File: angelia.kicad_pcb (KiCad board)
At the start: 2 copper layers, 160 x 120 mm, 206 parts, among them J10 Conn_Coaxial, J15 Conn_02x05_Top_Bottom, J16 Conn_02x13_Top_Bottom, J18 Conn_02x05_Top_Bottom, J25 Conn_Coaxial, J3 Conn_Coaxial, J5 Conn_Coaxial, P1 Conn_02x05_Top_Bottom, P2 Conn_02x05_Top_Bottom, U10 LTC2208xUP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

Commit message: all decoupling done
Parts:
- C104, C124, C141, C15, C189, C19, C190, C208, C230, C235, C236, C237, C238, C240, C241, C26, C53, C69, C71, C85, C86: moved to B.Cu
- moved C154 184.5 mm to (68.2, 118.4)
- moved C157 183.1 mm to (68.0, 121.4)
- moved C155 183.0 mm to (68.2, 115.6)
- moved C162 175.6 mm to (88.0, 113.6)
- moved C163 172.7 mm to (88.0, 109.0)
- moved C218 164.9 mm to (93.7, 122.2)
- moved C233 160.5 mm to (116.2, 131.2)
- moved C183 155.5 mm to (104.4, 124.8)
- moved C197 153.1 mm to (103.2, 128.8), turned to 90 degrees
- moved C193 150.9 mm to (104.4, 122.2)
- moved C95 150.4 mm to (86.2, 81.4), turned to 90 degrees
- moved C96 148.0 mm to (88.4, 81.4), turned to 90 degrees
- moved C225 141.2 mm to (159.4, 145.6)
- moved C211 126.9 mm to (158.2, 149.2), turned to 90 degrees
- moved C230 122.1 mm to (172.4, 140.6), turned to 180 degrees
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
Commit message: beginning special components
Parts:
- removed R1: R_Small, Resistor_SMD:R_0805_2012Metric
- added C103: 1n, Capacitor_SMD:C_0805_2012Metric, F.Cu at (254.3, 61.0)
- added C105: 100p, Capacitor_SMD:C_0805_2012Metric, F.Cu at (254.3, 64.0)
- added C107: 1n, Capacitor_SMD:C_0805_2012Metric, F.Cu at (258.8, 46.0)
- added C121: 10n, Capacitor_SMD:C_0402_1005Metric, B.Cu at (152.2, 66.2)
- added C130: 10n, Capacitor_SMD:C_0402_1005Metric, B.Cu at (129.0, 72.6)
- added C131: 10n, Capacitor_SMD:C_0402_1005Metric, B.Cu at (142.0, 71.7)
- added C136: 10n, Capacitor_SMD:C_0402_1005Metric, B.Cu at (153.6, 71.8)
- added C140: 10n, Capacitor_SMD:C_0402_1005Metric, B.Cu at (129.0, 71.2)
- added C165: 10u, Capacitor_SMD:C_0805_2012Metric, F.Cu at (258.8, 49.0)
- added C170: 1n, Capacitor_SMD:C_0805_2012Metric, F.Cu at (258.8, 52.0)
- added C172: 1n, Capacitor_SMD:C_0805_2012Metric, F.Cu at (258.8, 55.0)
- added C173: 100p, Capacitor_SMD:C_0805_2012Metric, F.Cu at (258.8, 58.0)
- added C175: 100p, Capacitor_SMD:C_0805_2012Metric, F.Cu at (258.8, 61.0)
- added C176: 10u, Capacitor_SMD:C_0805_2012Metric, F.Cu at (258.8, 64.0)
- added C178: 10u, Capacitor_SMD:C_0805_2012Metric, F.Cu at (263.2, 46.0)
- added C179: 1n, Capacitor_SMD:C_0805_2012Metric, F.Cu at (263.2, 49.0)
- added C180: 1n, Capacitor_SMD:C_0805_2012Metric, F.Cu at (263.2, 52.0)
- added C181: 10u, Capacitor_SMD:C_0805_2012Metric, F.Cu at (263.2, 55.0)
- added C184: 10u, Capacitor_SMD:C_0805_2012Metric, F.Cu at (263.2, 58.0)
- added C186: 10u, Capacitor_SMD:C_0805_2012Metric, F.Cu at (263.2, 61.0)
- added C195: 10u, Capacitor_SMD:C_0805_2012Metric, F.Cu at (263.2, 64.0)
- added C206: 100p, Capacitor_SMD:C_0805_2012Metric, F.Cu at (267.7, 46.0)
- added C239: 1n, Capacitor_SMD:C_0805_2012Metric, F.Cu at (267.7, 49.0)
- added C242: 1n, Capacitor_SMD:C_0805_2012Metric, F.Cu at (267.7, 52.0)
- added C251: 1n, Capacitor_SMD:C_0805_2012Metric, F.Cu at (267.7, 55.0)
- added C42: 10n, Capacitor_SMD:C_0402_1005Metric, B.Cu at (135.6, 71.8)
- added C59: 10n, Capacitor_SMD:C_0402_1005Metric, B.Cu at (124.2, 94.2)
- added C70: 1n, Capacitor_SMD:C_0805_2012Metric, F.Cu at (254.3, 46.0)
- added C72: 1n, Capacitor_SMD:C_0805_2012Metric, F.Cu at (254.3, 49.0)
- added C73: 1n, Capacitor_SMD:C_0805_2012Metric, F.Cu at (254.3, 52.0)
- added C75: 100p, Capacitor_SMD:C_0805_2012Metric, F.Cu at (254.3, 55.0)
- added C82: 10n, Capacitor_SMD:C_0402_1005Metric, B.Cu at (147.0, 95.2)
- added C87: 100p, Capacitor_SMD:C_0805_2012Metric, F.Cu at (254.3, 58.0)
- added D10: LED_Small, LED_SMD:LED_0805_2012Metric, F.Cu at (152.8, 130.0)
- added D11: LED_Small, LED_SMD:LED_0805_2012Metric, F.Cu at (150.6, 130.0)
- added D12: LED_Small, LED_SMD:LED_0805_2012Metric, F.Cu at (145.2, 130.0)
- added D13: LED_Small, LED_SMD:LED_0805_2012Metric, F.Cu at (142.8, 130.0)
- added D14: LED_Small, LED_SMD:LED_0805_2012Metric, F.Cu at (147.8, 130.0)
- added D15: LED_Small, LED_SMD:LED_0805_2012Metric, F.Cu at (140.2, 130.0)
- added D16: LED_Small, LED_SMD:LED_0805_2012Metric, F.Cu at (137.8, 130.0)
- added D17: LED_Small, LED_SMD:LED_0805_2012Metric, F.Cu at (135.2, 130.0)
- added D18: LED_Small, LED_SMD:LED_0805_2012Metric, F.Cu at (132.6, 130.0)
- added D19: LED_Small, LED_SMD:LED_0805_2012Metric, F.Cu at (130.0, 130.0)
- added F1: Fuse_Small, Fuse_smd:Fuse_1812_4532Metric, F.Cu at (158.4, 132.6)
- added F2: Fuse_Small, Fuse_smd:Fuse_1812_4532Metric, F.Cu at (168.4, 132.6)
- added F3: Fuse_Small, Fuse_smd:Fuse_1812_4532Metric, F.Cu at (115.1, 127.6)
- added F4: Fuse_Small, Fuse_smd:Fuse_1812_4532Metric, F.Cu at (118.0, 116.6)
- added F5: Fuse_Small, Fuse_smd:Fuse_1812_4532Metric, F.Cu at (142.8, 145.0)
- added J7: RJ45, Connector_RJ:RJ45_Amphenol_54602-x08_Horizontal, F.Cu at (68.0, 100.8)
- added L26: FerriteBead_Small, Ferrite_LC_NFM41P:Ferrite_LC_NFM41P, F.Cu at (93.7, 132.6)
- added L29: FerriteBead_Small, Ferrite_LC_NFM41P:Ferrite_LC_NFM41P, F.Cu at (104.7, 132.8)
- added L31: FerriteBead_Small, Ferrite_LC_NFM41P:Ferrite_LC_NFM41P, F.Cu at (105.0, 116.5)
- added L35: FerriteBead_Small, Ferrite_LC_NFM41P:Ferrite_LC_NFM41P, F.Cu at (108.6, 116.5)
- added L36: FerriteBead_Small, Ferrite_LC_NFM41P:Ferrite_LC_NFM41P, F.Cu at (94.8, 116.7)
- added L37: FerriteBead_Small, Ferrite_LC_NFM41P:Ferrite_LC_NFM41P, F.Cu at (98.2, 116.7)
- added L39: FerriteBead_Small, Ferrite_LC_NFM41P:Ferrite_LC_NFM41P, F.Cu at (101.4, 116.7)

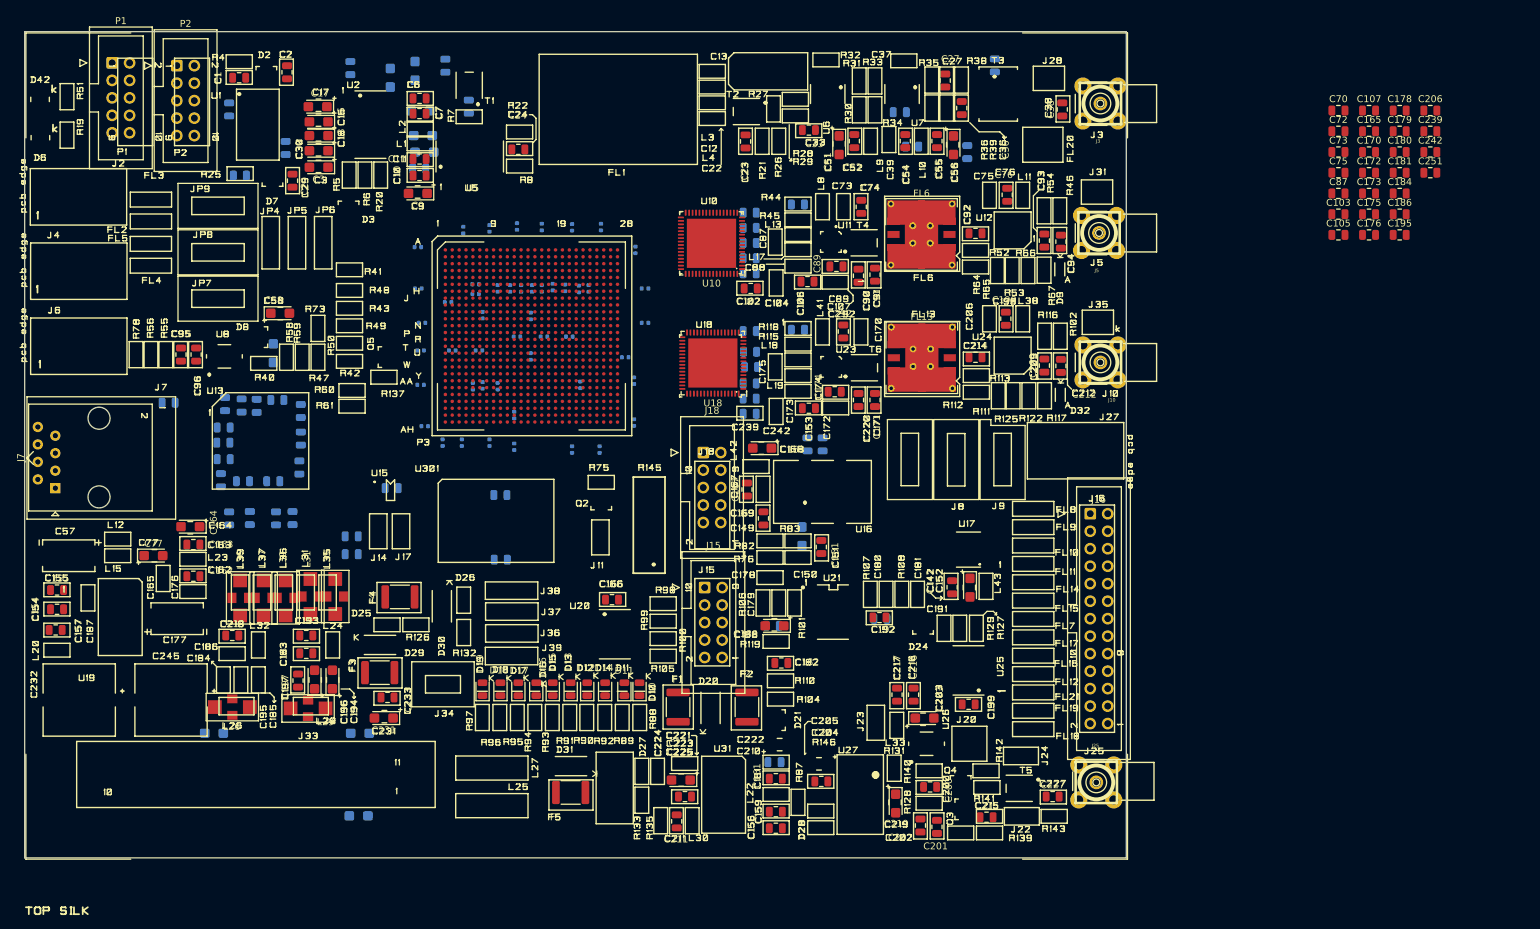
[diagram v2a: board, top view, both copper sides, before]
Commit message: some more caps, still some more caps and RJ45
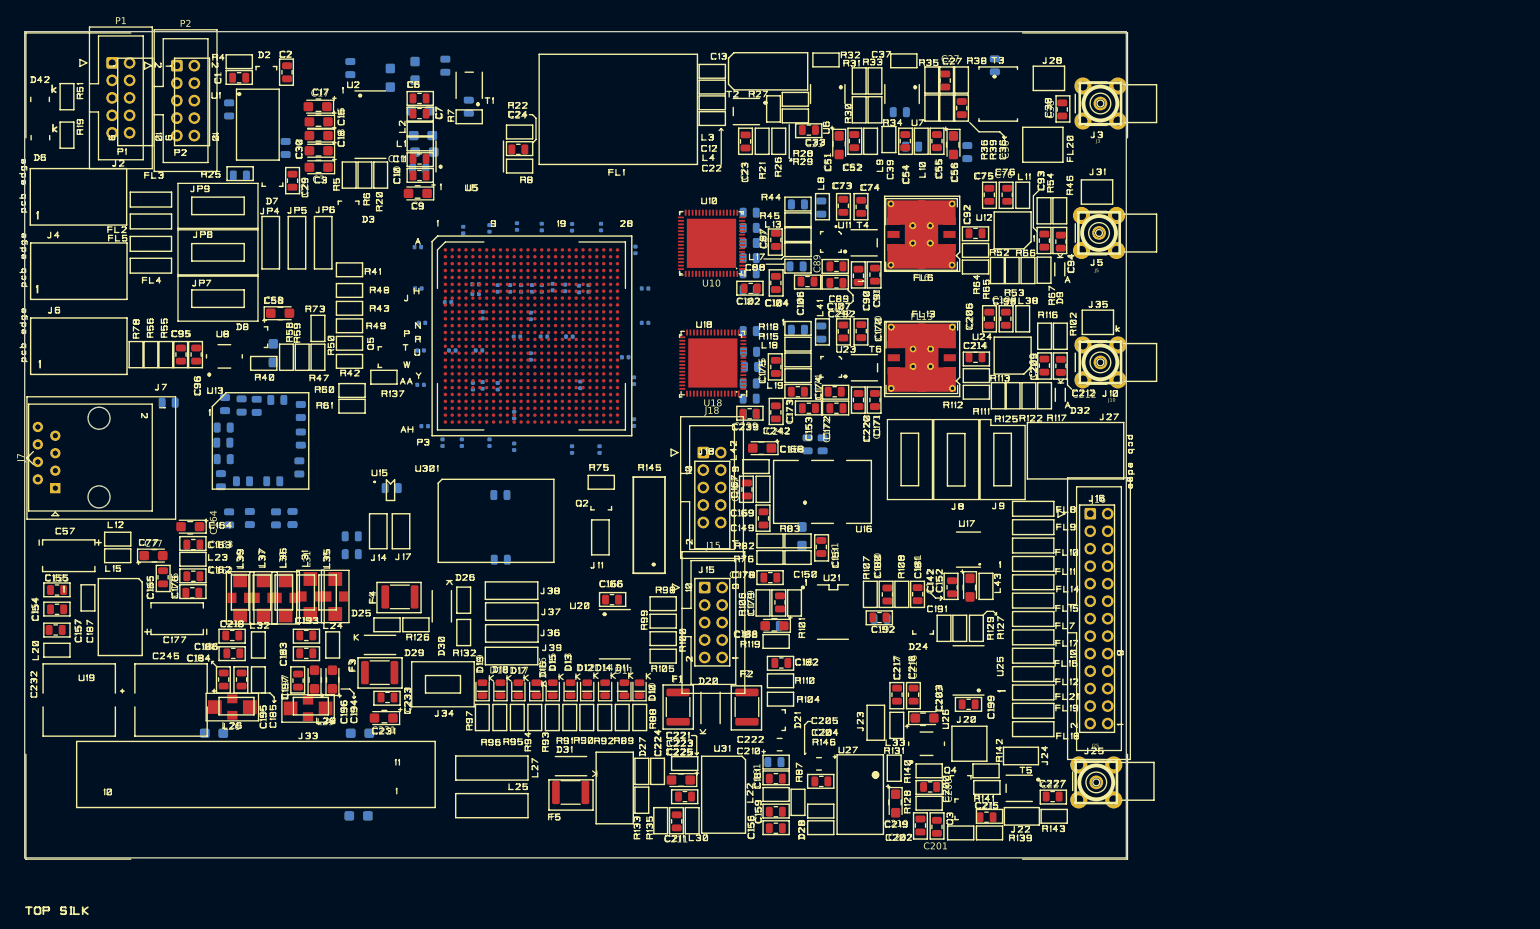
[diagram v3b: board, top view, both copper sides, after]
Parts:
- C103, C105, C251, C70, C72: moved to B.Cu
- C104: moved to F.Cu
- moved C165 186.8 mm to (83.6, 113.8), turned to 90 degrees
- moved C184 184.8 mm to (92.4, 128.6), turned to 90 degrees
- moved C186 181.0 mm to (93.8, 124.8)
- moved C195 180.2 mm to (95.0, 128.6), turned to 90 degrees
- moved C176 178.6 mm to (87.8, 116.0)
- moved C178 113.8 mm to (171.8, 113.8)
- moved C179 113.1 mm to (173.2, 117.4), turned to 90 degrees
- moved C239 107.0 mm to (168.8, 90.0)
- moved C242 102.3 mm to (172.6, 89.8), turned to 90 degrees
- moved C180 98.3 mm to (188.8, 116.2), turned to 90 degrees
- moved C181 93.0 mm to (193.2, 116.2), turned to 90 degrees
- moved C251 91.4 mm to (179.2, 78.2), turned to 90 degrees
- moved C175 89.0 mm to (172.6, 83.2), turned to 90 degrees
- moved C173 87.8 mm to (175.8, 86.8), turned to 180 degrees
- moved C70 87.2 mm to (168.8, 63.0), turned to 180 degrees
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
